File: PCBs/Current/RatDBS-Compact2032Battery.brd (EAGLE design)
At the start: 25.4 x 19.1 mm, 20 parts

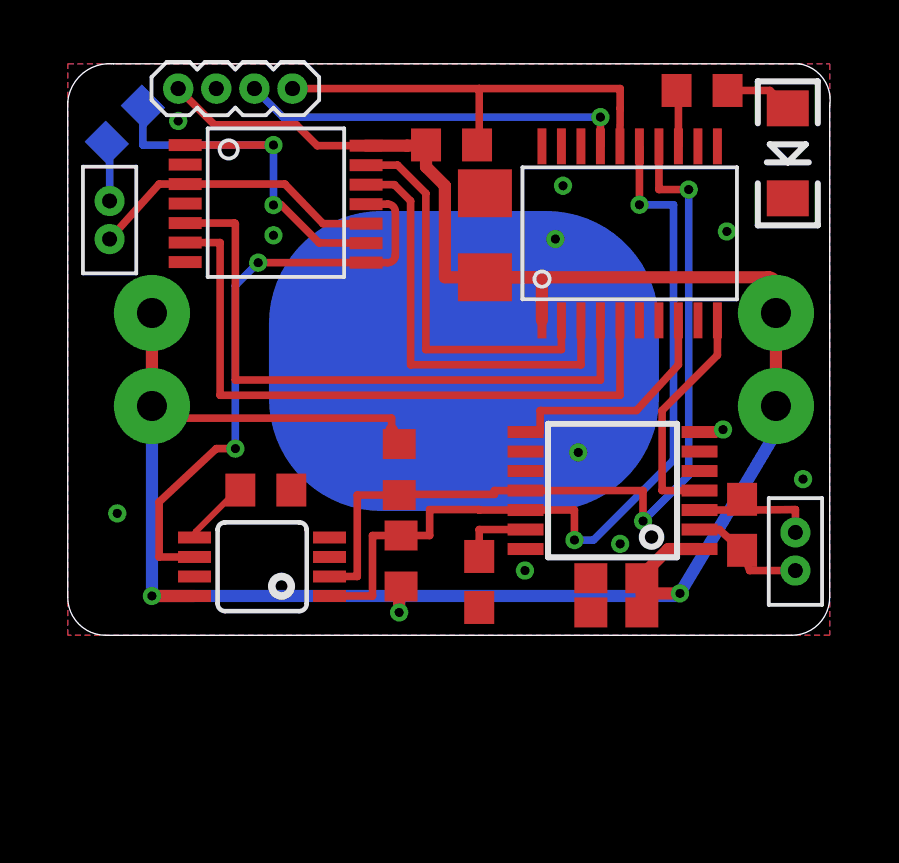
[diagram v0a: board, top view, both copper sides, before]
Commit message: Added an error state until NFC is read correctly.
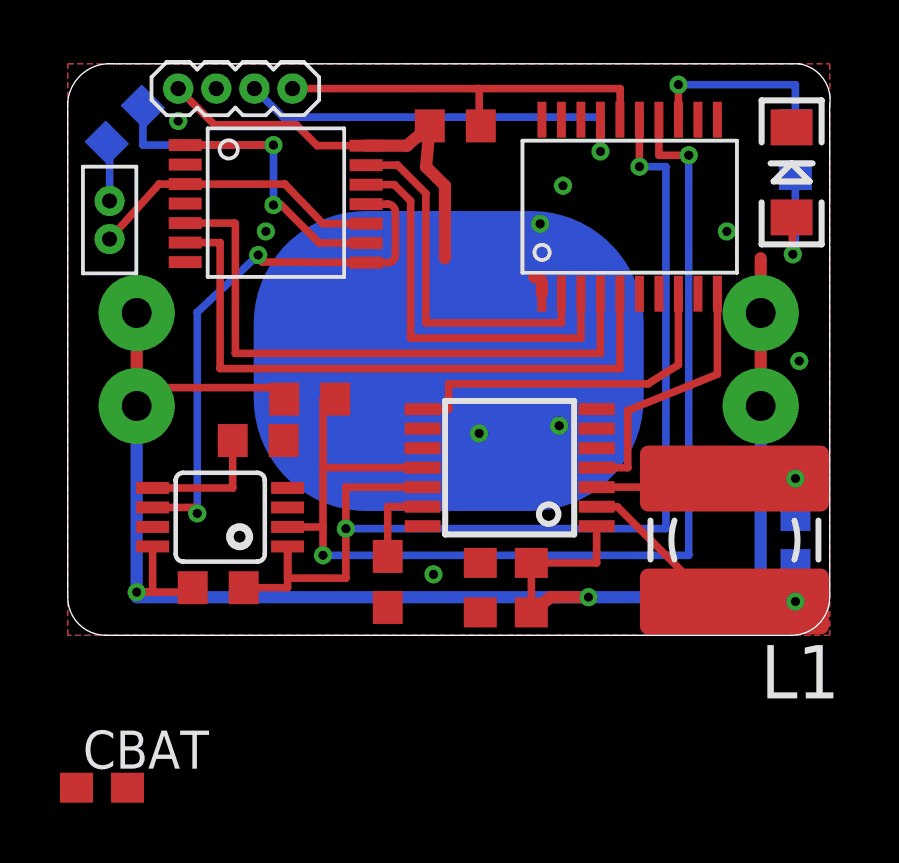
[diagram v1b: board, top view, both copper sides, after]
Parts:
- removed ANT: FTSH-102, Samtec50Mil:FTSH-102-DH
- added L1: (no value), rcl:POWER-CHOKE_WE-TPC
- C1: value 1µ -> 1u
- C2: value 0.1µ -> 0.1u
- CBAT: value 10µ -> 10u; device rcl:C1206 -> rcl:C0603
- C_VC: value 0.47µ -> 0.47u
- moved CBAT 22.4 mm to (1.14, -5.08), turned to 0 degrees
- moved R1_I2C 6.16 mm to (5.02, 1.59), turned to 180 degrees
- moved R2_I2C 3.80 mm to (8.06, 7.87), turned to 180 degrees
- moved C1 3.72 mm to (14.6, 2.41)
- moved C2 3.68 mm to (14.6, 0.76)
- moved R_LED 3.68 mm to (24.3, 16.2), flipped to the bottom, turned to 270 degrees
- moved U$1 3.51 mm to (14.7, 5.59)
- moved C_VC 3.05 mm to (10.7, 1.78)
- moved DS4432U+ 2.16 mm to (5.08, 3.94)
- moved CANT 1.85 mm to (24.3, 3.17), flipped to the bottom
- moved R_INPUT_FS0 1.67 mm to (6.35, 6.49)
- moved MSP430 0.89 mm to (18.7, 14.3)
- moved R_PULLUP_RST 0.65 mm to (12.9, 17.0)
- moved LED6 0.65 mm to (24.1, 15.4), turned to 90 degrees
- moved BAT1 0.51 mm to (12.7, 9.14)
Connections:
- net GND: now also CBAT.2; no longer CBAT.1
- net N$12: now also L1.2; no longer ANT.P$1
- net N$2: now also L1.1; no longer ANT.P$2
- net VDD: now also CBAT.1; no longer CBAT.2
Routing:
- net VDD: track 84.0 -> 74.4 mm, vias 3 -> 2
- net SCL: track 28.4 -> 37.8 mm
- net SDA: track 28.1 -> 36.6 mm
- net N$2: track 3.93 -> 9.14 mm, vias 0 -> 1
- net N$5: track 1.87 -> 6.38 mm, vias 0 -> 1
- net N$3: track 7.97 -> 11.9 mm
- net N$12: track 4.40 -> 8.11 mm, vias 0 -> 1
- net N$8: track 2.28 -> 4.25 mm
- net N$9: track 2.25 -> 3.96 mm, vias 0 -> 1
- net _RST: track 15.0 -> 13.7 mm
- net TEST: track 12.9 -> 14.2 mm
- net STIM_IN: track 20.0 -> 18.8 mm
- net N$7: track 7.69 -> 8.85 mm
- net IN4: track 14.3 -> 13.4 mm
- net IN3: track 22.1 -> 21.2 mm
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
